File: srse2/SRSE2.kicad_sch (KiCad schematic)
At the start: 88 parts, among them J1 s88-N, J2 CAN, P1 I2S, P10 PIC_SPARE, P11 RS485 TERM, P12 RS485, P13 CONN_01X03, P15 S88I, P17 RA5, P18 CONN_01X03, P19 CONN_01X02, P2 CONN_01X09, P20 O2P-Rst, P3 CONN_01X02, P4 CONN_01X04, P5 CONN_01X04, P6 ISO_I2C, P7 CAN_TERM, P8 CAN, P9 PIC_I2C, U1 Omega2, U10 OKI-78SR, U2 ADuM1250, U3 SN65HVD230, U4 PIC18F25K80, U5 HR911105A, U6 MAX485, U7 TPS5430DDA, U8 CD4504, U9 LM317, Y1 16MHz

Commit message: new SRSEII JLCPCB production files Version 1.8
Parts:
- C5: LCSC C19702 -> C13585
- R104, R105: LCSC (none) -> C17888; LCSDC C17888 -> (none)
- U2, U6: footprint w_smd_dil:so-8 -> Package_SO:SOIC-8_3.9x4.9mm_P1.27mm
- U8: footprint w_smd_dil:so-16 -> Package_SO:SO-16_3.9x9.9mm_P1.27mm
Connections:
- net Vout: now reaches C102.1, L100.2, R101.1, R105.1
- net PH: now reaches C101.2, D100.1 (K), L100.1, U7.8 (PH)
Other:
- moved on the sheet: C18
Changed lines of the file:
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@@
   (title_block
     (title "Smallest Rocrail Server Ever II")
-    (date "2022-10-21")
+    (date "2022-11-07")
     (rev "1.8")
     (company "Gerhard Bertelsmann")
@@
     (stroke (width 0) (type default) (color 0 0 0 0))
   )
+  (wire (pts (xy 45.72 121.285) (xy 45.72 118.745))
+    (stroke (width 0) (type default) (color 0 0 0 0))
+  )
   (wire (pts (xy 217.805 113.03) (xy 220.345 113.03))
     (stroke (width 0) (type default) (color 0 0 0 0))
@@
     (stroke (width 0) (type default) (color 0 0 0 0))
   )
-  (wire (pts (xy 45.72 126.365) (xy 45.72 127))
+  (wire (pts (xy 45.72 128.905) (xy 45.72 131.445))
     (stroke (width 0) (type default) (color 0 0 0 0))
   )
@@
     (effects (font (size 1.524 1.524)) (justify left bottom))
   )
+  (label "PH" (at 330.2 173.99 0)
+    (effects (font (size 1.524 1.524)) (justify left bottom))
+  )
   (label "RxD" (at 115.57 77.47 0)
     (effects (font (size 1.524 1.524)) (justify left bottom))
@@
     (effects (font (size 1.524 1.524)) (justify left bottom))
   )
+  (label "Vout" (at 358.14 168.91 0)
+    (effects (font (size 1.524 1.524)) (justify left bottom))
+  )
   (label "RxD" (at 232.41 236.22 180)
     (effects (font (size 1.524 1.524)) (justify right bottom))
@@
       (effects (font (size 1.27 1.27)) (justify left))
     )
-    (property "Footprint" "w_smd_dil:so-8" (id 2) (at 66.675 247.65 0)
+    (property "Footprint" "Package_SO:SOIC-8_3.9x4.9mm_P1.27mm" (id 2) (at 66.675 247.65 0)
       (effects (font (size 1.27 1.27) italic) hide)
     )
@@
       (effects (font (size 1.27 1.27)) (justify left))
     )
-    (property "Footprint" "w_smd_dil:so-8" (id 2) (at 191.77 106.68 0)
+    (property "Footprint" "Package_SO:SOIC-8_3.9x4.9mm_P1.27mm" (id 2) (at 191.77 106.68 0)
       (effects (font (size 1.27 1.27) italic) hide)
     )
@@
     (property "Reference" "U8" (id 0) (at 114.935 137.795 0))
     (property "Value" "CD4504" (id 1) (at 128.905 137.795 0))
-    (property "Footprint" "w_smd_dil:so-16" (id 2) (at 122.555 193.04 0)
+    (property "Footprint" "Package_SO:SO-16_3.9x9.9mm_P1.27mm" (id 2) (at 122.555 193.04 0)
       (effects (font (size 1.27 1.27)) hide)
     )
@@
   (symbol (lib_id "Device:R") (at 55.88 123.825 180) (unit 1)
     (in_bom yes) (on_board yes)
-    (property "Reference" "R26" (id 0) (at 53.975 124.46 90))
+    (property "Reference" "R26" (id 0) (at 53.975 125.73 90))
     (property "Value" "240" (id 1) (at 55.88 123.825 90))
     (property "Footprint" "Resistors_SMD:R_0805_HandSolderingII" (id 2) (at 57.658 123.825 0)
@@
     (pin "2")
   )
-  (symbol (lib_id "power:GND") (at 45.72 127 0) (unit 1)
+  (symbol (lib_id "power:GND") (at 45.72 131.445 0) (unit 1)
     (in_bom yes) (on_board yes)
-    (property "Reference" "#PWR0102" (id 0) (at 45.72 133.35 0)
+    (property "Reference" "#PWR0102" (id 0) (at 45.72 137.795 0)
       (effects (font (size 1.27 1.27)) hide)
     )
-    (property "Value" "GND" (id 1) (at 45.72 130.81 0))
-    (property "Footprint" "" (id 2) (at 45.72 127 0))
-    (property "Datasheet" "" (id 3) (at 45.72 127 0))
+    (property "Value" "GND" (id 1) (at 45.72 135.255 0))
+    (property "Footprint" "" (id 2) (at 45.72 131.445 0))
+    (property "Datasheet" "" (id 3) (at 45.72 131.445 0))
     (pin "1")
   )
@@
       (effects (font (size 1.27 1.27)) hide)
     )
-    (property "LCSC" "C19702" (id 4) (at 171.45 255.27 0)
+    (property "LCSC" "C13585" (id 4) (at 171.45 255.27 0)
       (effects (font (size 1.524 1.524)) hide)
     )
@@
     (pin "2")
   )
-  (symbol (lib_id "Device:C") (at 45.72 122.555 0) (unit 1)
-    (in_bom yes) (on_board yes) (fields_autoplaced)
-    (property "Reference" "C18" (id 0) (at 49.53 121.2849 0)
+  (symbol (lib_id "Device:C") (at 45.72 125.095 0) (unit 1)
+    (in_bom yes) (on_board yes)
+    (property "Reference" "C18" (id 0) (at 38.735 123.825 0)
       (effects (font (size 1.27 1.27)) (justify left))
     )
-    (property "Value" "10uF" (id 1) (at 49.53 123.8249 0)
+    (property "Value" "10uF" (id 1) (at 38.735 126.365 0)
       (effects (font (size 1.27 1.27)) (justify left))
     )
-    (property "Footprint" "Capacitor_SMD:C_1206_3216Metric_Pad1.33x1.80mm_HandSolder" (id 2) (at 46.6852 126.365 0)
+    (property "Footprint" "Capacitor_SMD:C_1206_3216Metric_Pad1.33x1.80mm_HandSolder" (id 2) (at 46.6852 128.905 0)
       (effects (font (size 1.27 1.27)) hide)
     )
-    (property "Datasheet" "~" (id 3) (at 45.72 122.555 0)
+    (property "Datasheet" "~" (id 3) (at 45.72 125.095 0)
       (effects (font (size 1.27 1.27)) hide)
     )
-    (property "LCSC" "C13585" (id 4) (at 45.72 122.555 0)
+    (property "LCSC" "C13585" (id 4) (at 45.72 125.095 0)
       (effects (font (size 1.524 1.524)) hide)
     )
@@
       (effects (font (size 1.27 1.27)) hide)
     )
-    (property "LCSDC" "C17888" (id 4) (at 285.75 168.91 90)
+    (property "LCSC" "C17888" (id 4) (at 285.75 168.91 90)
       (effects (font (size 1.524 1.524)) hide)
     )
@@
       (effects (font (size 1.27 1.27)) hide)
     )
-    (property "LCSDC" "C17888" (id 4) (at 374.65 168.91 90)
+    (property "LCSC" "C17888" (id 4) (at 374.65 168.91 90)
       (effects (font (size 1.524 1.524)) hide)
     )
@@
     )
     (path "/00000000-0000-0000-0000-000057c0fc99"
-      (reference "U2") (unit 1) (value "ADuM1250") (footprint "w_smd_dil:so-8")
+      (reference "U2") (unit 1) (value "ADuM1250") (footprint "Package_SO:SOIC-8_3.9x4.9mm_P1.27mm")
     )
     (path "/00000000-0000-0000-0000-000061a9fb75"
@@
     )
     (path "/00000000-0000-0000-0000-000057c05375"
-      (reference "U6") (unit 1) (value "MAX485") (footprint "w_smd_dil:so-8")
+      (reference "U6") (unit 1) (value "MAX485") (footprint "Package_SO:SOIC-8_3.9x4.9mm_P1.27mm")
     )
     (path "/11e404aa-452d-4ebe-9eae-3791d3f90f12"
@@
     )
     (path "/00000000-0000-0000-0000-000061f1f29f"
-      (reference "U8") (unit 1) (value "CD4504") (footprint "w_smd_dil:so-16")
+      (reference "U8") (unit 1) (value "CD4504") (footprint "Package_SO:SO-16_3.9x9.9mm_P1.27mm")
     )
     (path "/00000000-0000-0000-0000-00006375e633"

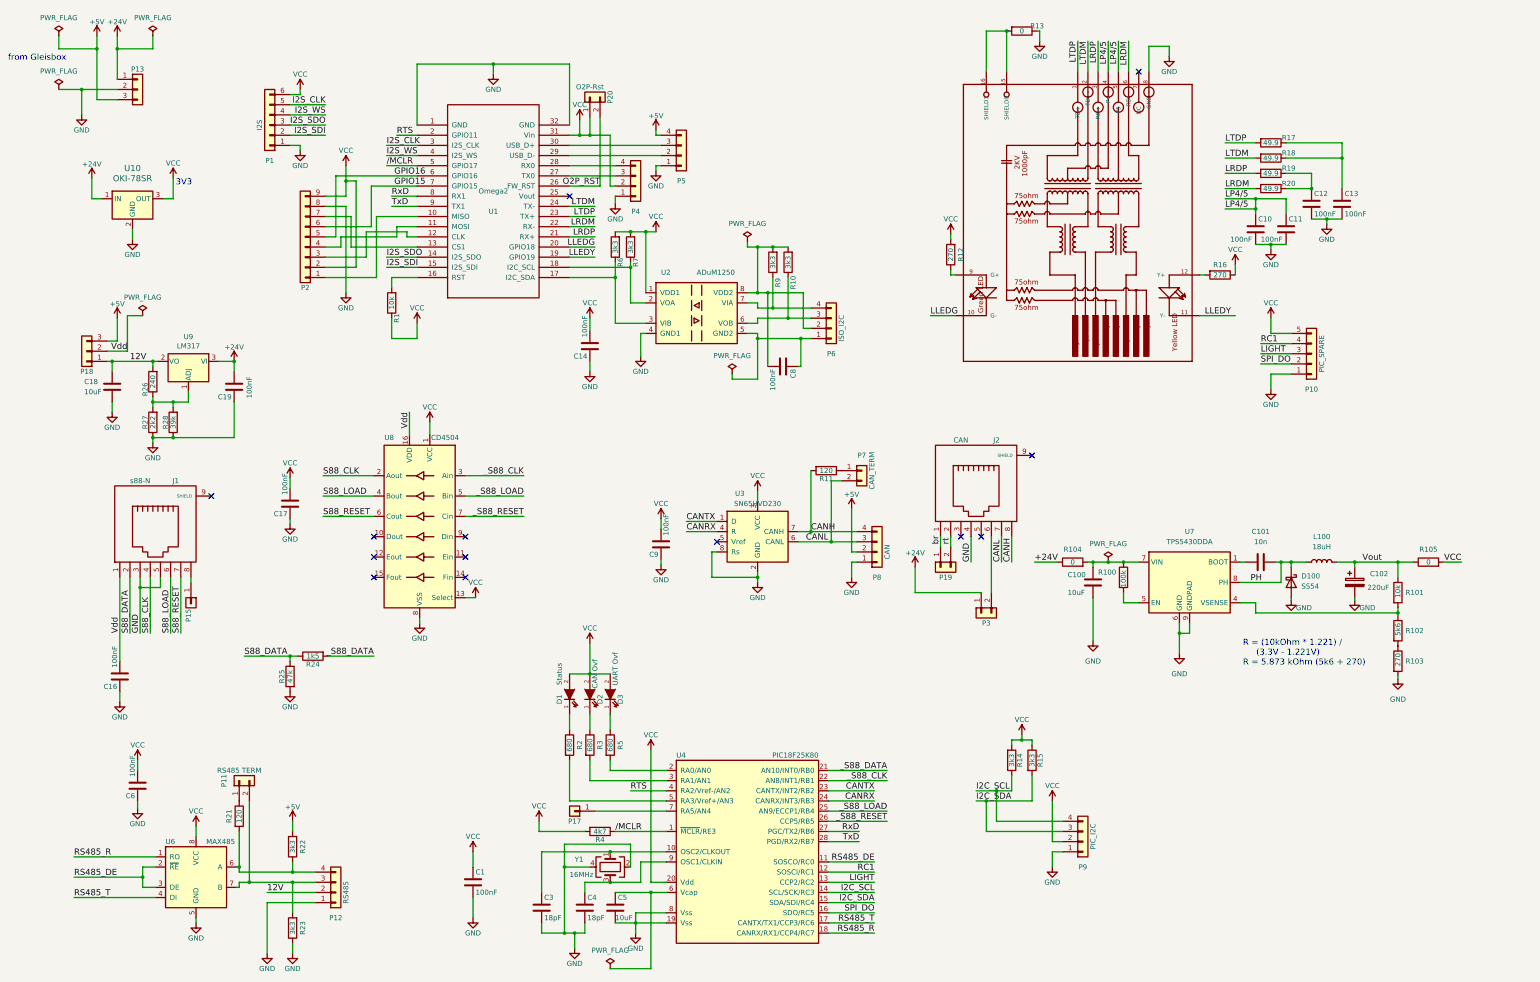
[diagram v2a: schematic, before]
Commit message: remove old 3V3 DCDC
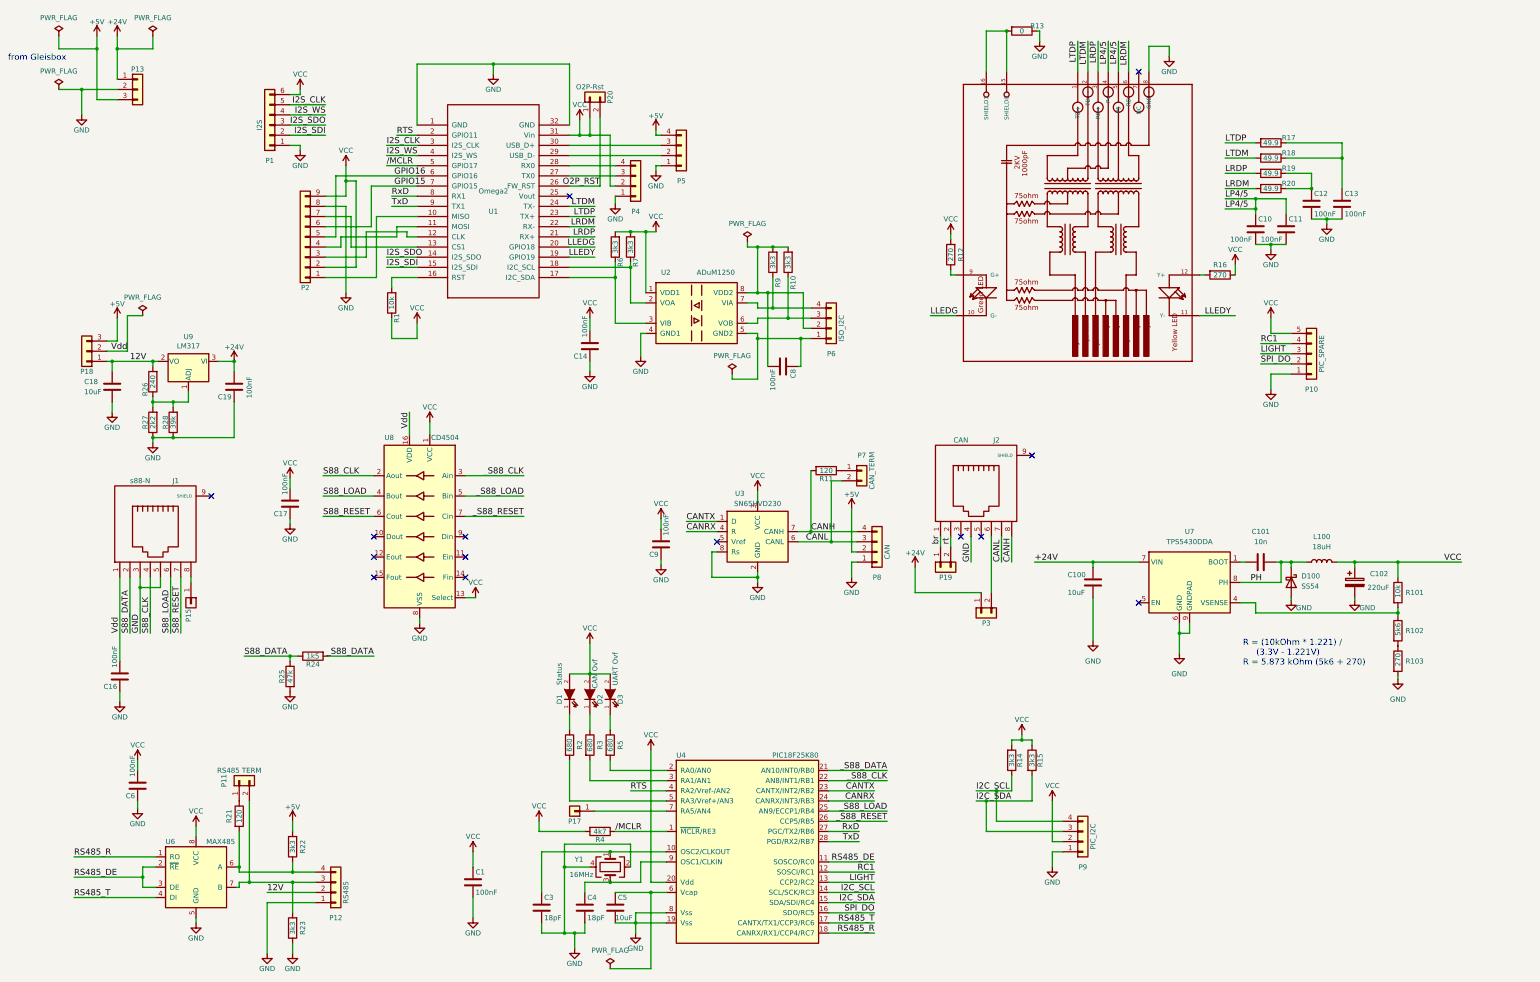
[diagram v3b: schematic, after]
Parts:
- removed R100: 100k, Resistor_SMD:R_0603_1608Metric, symbol Device:R
- removed R104, R105: 0, Resistor_SMD:R_1206_3216Metric_Pad1.30x1.75mm_HandSolder, symbol Device:R
- removed U10: OKI-78SR, common-ICs:OKI-78SR, symbol Converter_DCDC:OKI-78SR-3.3_1.5-W36-C
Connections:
- net Vout is gone; now on net VCC: C102.1, L100.2, R101.1
- net +24V: now also C100.2, U7.7 (VIN)
- no-connect marks 13 -> 14
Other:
- note removed: "3V3"

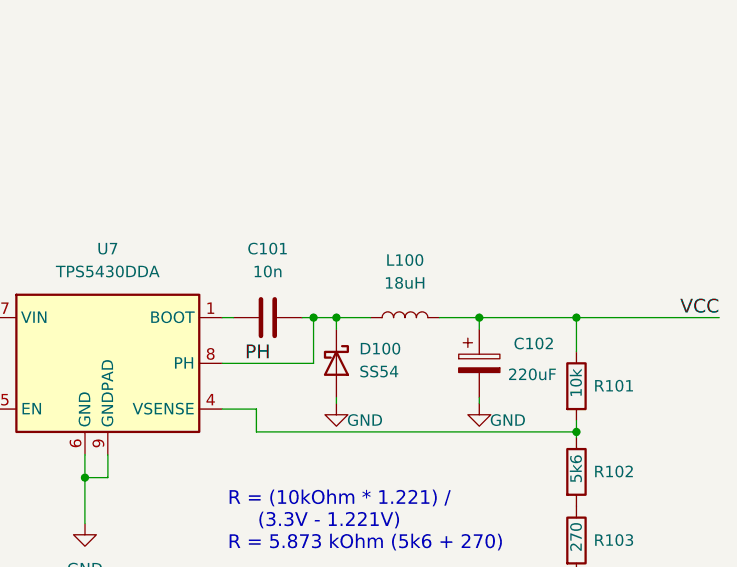
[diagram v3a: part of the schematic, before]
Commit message: change LCSC ordering number for L100 15uH
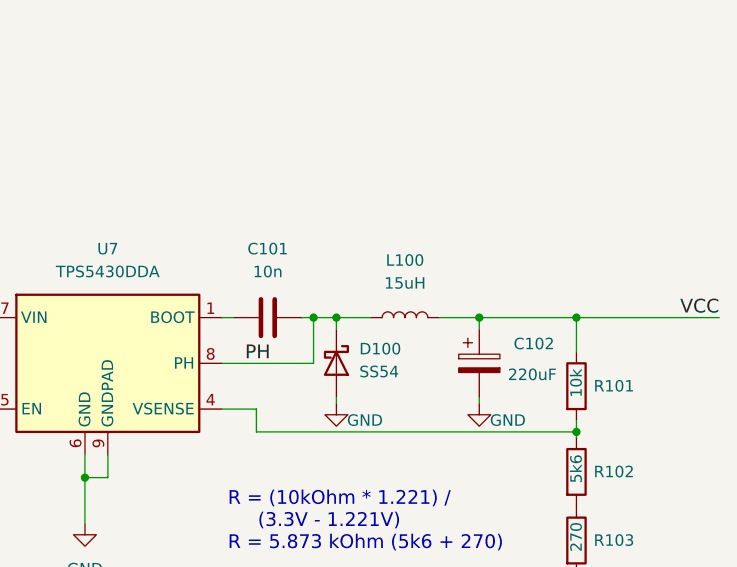
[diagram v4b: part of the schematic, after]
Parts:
- L100: value 18uH -> 15uH; LCSC C225049 -> C225048
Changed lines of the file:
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@@
     (in_bom yes) (on_board yes) (fields_autoplaced)
     (property "Reference" "L100" (id 0) (at 347.98 162.56 90))
-    (property "Value" "18uH" (id 1) (at 347.98 165.1 90))
+    (property "Value" "15uH" (id 1) (at 347.98 165.1 90))
     (property "Footprint" "Inductor_SMD:L_10.4x10.4_H4.8" (id 2) (at 347.98 168.91 0)
       (effects (font (size 1.27 1.27)) hide)
@@
       (effects (font (size 1.27 1.27)) hide)
     )
-    (property "LCSC" "C225049" (id 4) (at 347.98 168.91 90)
+    (property "LCSC" "C225048" (id 4) (at 347.98 168.91 90)
       (effects (font (size 1.524 1.524)) hide)
     )
@@
     )
     (path "/ac4015fa-5ed9-43ef-8f0a-9cdc21f06b2c"
-      (reference "L100") (unit 1) (value "18uH") (footprint "Inductor_SMD:L_10.4x10.4_H4.8")
+      (reference "L100") (unit 1) (value "15uH") (footprint "Inductor_SMD:L_10.4x10.4_H4.8")
     )
     (path "/00000000-0000-0000-0000-000057c12a4e"
